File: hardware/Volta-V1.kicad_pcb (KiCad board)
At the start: 4 copper layers, 63.9 x 32 mm, 91 parts, among them SW1 TS-1088-AR02016, SW2 TS-1088-AR02016, U1 AMS1117-3.3, U2 CH32V317WCU6_C49188393, U3 SGL0622Z, U4 RDA5815M, X1 X50328MSB2GI, X2 Q13FC1350000400, X3 X49SD27MSD2SC

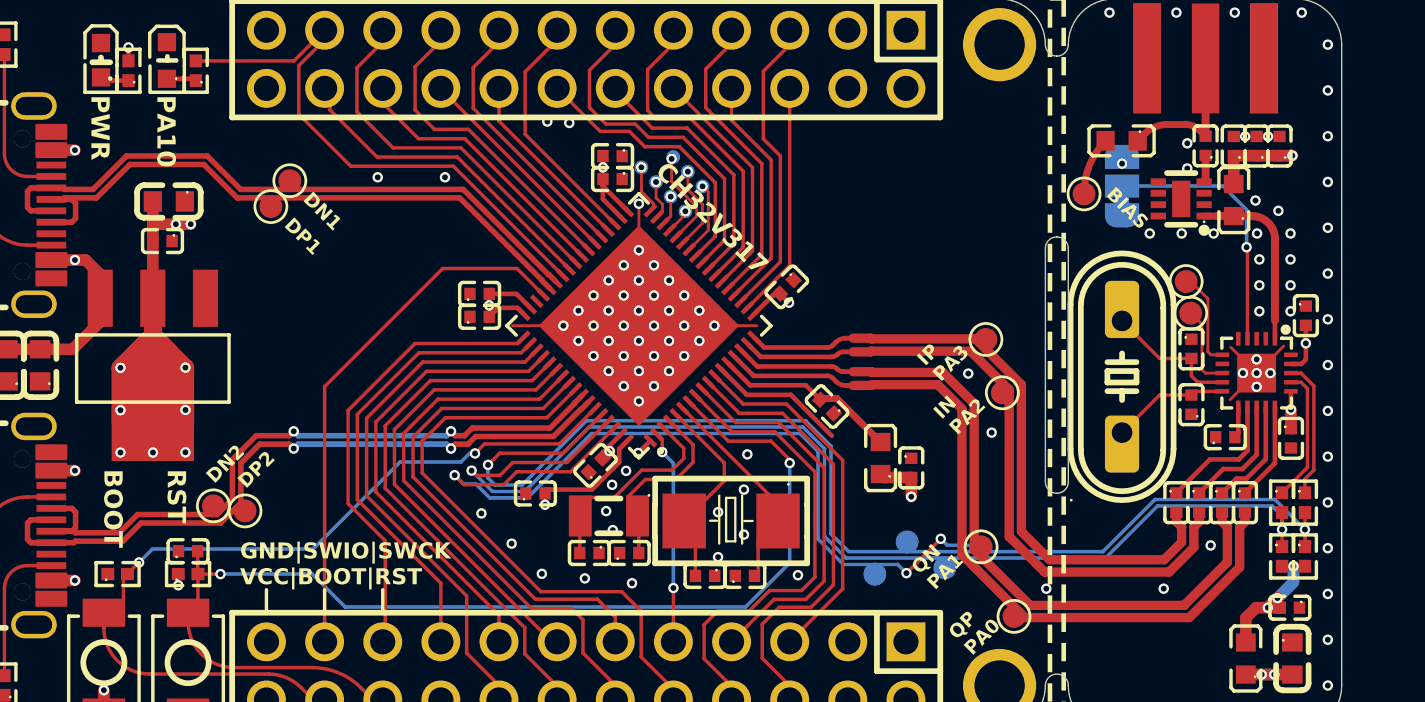
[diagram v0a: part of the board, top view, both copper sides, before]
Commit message: AGC pin is now wired.
also have added a programming header section in the GPIO header.
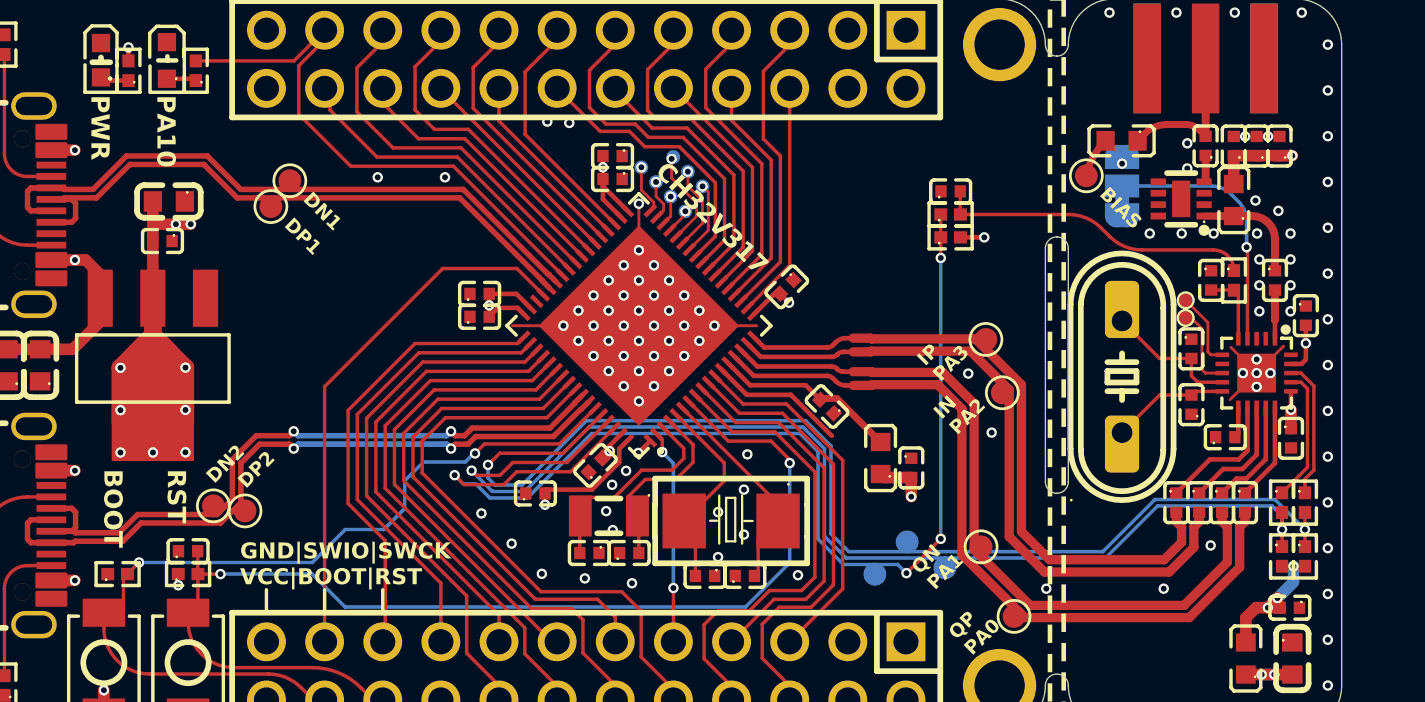
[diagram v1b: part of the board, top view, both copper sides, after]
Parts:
- added C28: 0402B102K500NT, lcsc:C0402, F.Cu at (171.8, 92.3)
- added C30: 0402B102K500NT, lcsc:C0402, F.Cu at (160.4, 88.4)
- added C36: CL05B104KO5NNNC, lcsc:C0402, F.Cu at (174.6, 92.3)
- added R14: 0402WGF2001TCE, lcsc:R0402, F.Cu at (160.4, 89.4)
- added R15: 0402WGF2001TCE, lcsc:R0402, F.Cu at (160.4, 90.4)
- added R9: 0402WGF2001TCE, lcsc:R0402, F.Cu at (172.8, 92.3)
- TP5: renamed from TP21; footprint TestPoint:TestPoint_Pad_D1.0mm -> lcsc:2xTinyTestPoint
- TP6: renamed from TP20; footprint TestPoint:TestPoint_Pad_D1.0mm -> lcsc:2xTinyTestPoint
- moved TP6 0.82 mm to (170.7, 93.2)
- moved TP21 0.80 mm to (166.4, 87.7)
- moved TP5 0.30 mm to (170.7, 93.9)
- renumbered C8 to C1, C21 to C10, C15 to C12, C1 to C15, C3 to C16, C4 to C17, C2 to C18, C31 to C19, C16 to C2, C22 to C20, C23 to C21, C24 to C22, C32 to C23, C28 to C24, C27 to C25, C25 to C27, C33 to C29, C9 to C3, C30 to C31, C12 to C32, C5 to C33, C6 to C34, C7 to C35, C17 to C4, C18 to C5, C29 to C6, C19 to C7, C10 to C8, C20 to C9, L3 to L1, L4 to L2, L1 to L3, L2 to L4, R7 to R1, R9 to R12, R8 to R13, R12 to R2, R5 to R4, R4 to R5, R1 to R7, R2 to R8, SW2 to SW1, SW1 to SW2, TP9 to TP10, TP14 to TP11, TP18 to TP12, TP8 to TP14, TP17 to TP15, TP7 to TP16, TP16 to TP17, TP5 to TP18, TP4 to TP19, TP11 to TP2, TP3 to TP20, TP6 to TP21, TP2 to TP3, TP12 to TP4, TP10 to TP7, TP15 to TP8, TP19 to TP9, U4 to U2, U2 to U3, U3 to U4
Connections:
- net GPIO_PE0 renamed RF_AGC
- L4 pad 1: RF_FEED -> Net-(U4-RF_OUT)
- U2 pad 5: unconnected-(U4-AGC-Pad5) -> Net-(U2-AGC)
- U4 pad 1: RF_FEED -> Net-(U4-RF_OUT)
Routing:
- net Net-(C30-Pad2): track 0.00 -> 13.9 mm
- net RF_AGC: track 38.2 -> 50.6 mm, vias 3 -> 4
- net RF_FEED: track 7.99 -> 2.13 mm
- net Net-(U4-RF_OUT): track 0.00 -> 5.02 mm
- net Net-(U2-AGC): track 0.00 -> 3.20 mm
- net +3.3V: track 84.3 -> 85.3 mm, vias 21 -> 22
- net Net-(U2-XOUT_EN): track 4.26 -> 3.34 mm
- net Net-(L3-Pad2): track 2.55 -> 1.78 mm
- net BOOT_BTN: track 37.5 -> 38.2 mm

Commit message: finalize v1 and upload related documents
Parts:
- moved C28 1.00 mm to (172.8, 92.3)
- moved R9 1.00 mm to (171.8, 92.3)
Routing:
- net Net-(C30-Pad2): track 13.9 -> 12.6 mm
